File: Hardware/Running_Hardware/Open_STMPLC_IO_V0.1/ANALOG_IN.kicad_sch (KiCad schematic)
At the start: 1 part, among them U39 AD4111

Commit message: Analog input section
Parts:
- added C64, C65, C82: 1uF, symbol Device:C_Small
- added C66, C67, C68, C81: 100nF, symbol Device:C_Small
- added C69, C74, C79, C80: 4.7nF, symbol Device:C_Small
- added C70, C73, C77, C78: 680pF, symbol Device:C_Small
- added C71, C72, C75, C76: 470pF, symbol Device:C_Small
- added C83, C84: 10pF, Capacitor_SMD:C_0603_1608Metric_Pad1.08x0.95mm_HandSolder, symbol Device:C_Small
- added D118, D121, D124, D125: SMAJ33CA, Diode_SMD:D_SMA, symbol Diode:SMAJ33CA
- added D119, D120, D122, D123: SMAJ10CA, Diode_SMD:D_SMA, symbol Diode:SMAJ33CA
- added D126, D127, D128: LED, symbol Device:LED_Small
- added F1, F2, F3, F4: MF-USMF005-2, symbol Device:Fuse_Small
- added J35, J36, J37, J38: Screw_Terminal_01x03, symbol Connector:Screw_Terminal_01x03
- added R190, R191: 0R, symbol Device:R_Small
- added R192, R194, R195, R196, R198, R199, R200, R201: 180R, symbol Device:R_Small
- added R193, R197, R202, R203: 1K, symbol Device:R_Small
- added R204, R205: 100K, symbol Device:R_Small
- added R206: 2.2K, symbol Device:R_Small
- added R207, R208: 4.7K, symbol Device:R_Small
- added TP1, TP2, TP3, TP4, TP5: TestPoint, symbol Connector:TestPoint
- added U40: REF3025, Package_TO_SOT_SMD:SOT-23, symbol Reference_Voltage:REF3025
- added Y2: 16MHz, Crystal:Crystal_SMD_5032-4Pin_5.0x3.2mm, symbol Device:Crystal_GND24
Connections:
- net GND: now reaches U39.1 (VINCOM)
- net GND: now also U39.21 (DGND), U39.30 (IIN3-), U39.31 (IIN2-), U39.32 (IIN1-), U39.33 (IIN0-), U39.41 (EP), U39.8 (AVSS), C64.2, C65.2, C66.2, C67.2, C68.2, C69.2, C71.1, C72.1, C74.2, C75.1, C76.1, C79.2, C80.2, C81.2, C82.2, C83.2, C84.2, D118.2 (A2), D119.1 (A1), D120.1 (A1), D121.2 (A2), D122.1 (A1), D123.1 (A1), D124.2 (A2), D125.2 (A2), J35.1 (Pin_1), J36.1 (Pin_1), J37.1 (Pin_1), J38.1 (Pin_1), R190.2, R191.2, U40.3 (GND), Y2.2, Y2.4
- net at U39.11 (VBIAS-): now also R190.1
- net XTAL1: now reaches U39.12 (XTAL1)
- net XTAL1: now also C83.1, Y2.3
- net XTAL2: now reaches U39.13 (XTAL2/CLKIO)
- net XTAL2: now also C84.1, Y2.1
- net ANALOG_IN_DOUT: now reaches U39.14 (DOUT/~{RDY})
- net ANALOG_IN_DOUT: now also R205.2
- net ANALOG_IN_DIN: now reaches U39.15 (DIN)
- net ANALOG_IN_SCLK: now reaches U39.16 (SCLK)
- net ANALOG_IN_CS: now reaches U39.17 (~{CS})
- net at U39.18 (~{ERROR}): now also D126.1 (K)
- net at U39.19 (~{SYNC}): now also R204.2
- net VIN0: now reaches U39.2 (VIN0)
- net VIN0: now also C69.1, C70.1, R192.1
- net at U39.20 (IOVDD): now also C67.1
- net at U39.22 (REGCAPD): now also C65.1
- net COMPA: now reaches U39.23 (COMPA)
- net COMPA: now also R193.1, R197.1, R202.1, R203.1
- net at U39.24 (COMPB): now also TP1.1
- net at U39.25 (GPO0): now also D127.1 (K)
- net VIN4: now reaches U39.26 (VIN4)
- net VIN4: now also C77.1, C79.1, R200.1
- net at U39.27 (VIN5): now also TP4.1
- net VIN6: now reaches U39.28 (VIN6)
- net VIN6: now also C78.1, C80.1, R201.1
- net at U39.29 (VIN7): now also TP5.1
- net at U39.3 (VIN1): now also TP2.1
- net IIN0+: now reaches U39.34 (IIN0+)
- net IIN0+: now also C71.2, R194.1
- net IIN1+: now reaches U39.35 (IIN1+)
- net IIN1+: now also C72.2, R195.1
- net IIN2+: now reaches U39.36 (IIN2+)
- net IIN2+: now also C75.2, R198.1
- net IIN3+: now reaches U39.37 (IIN3+)
- net IIN3+: now also C76.2, R199.1
- net at U39.38 (GPO1): now also D128.1 (K)
- net at U39.39 (REF-): now also R191.1
- net VIN2: now reaches U39.4 (VIN2)
- net VIN2: now also C73.1, C74.1, R196.1
- net REF+: now reaches U39.40 (REF+)
- net REF+: now also C81.1, C82.1, U40.2 (OUT)
- net at U39.5 (VIN3): now also TP3.1
- net at U39.6 (REFOUT): now also C68.1
- net at U39.7 (REGCAPA): now also C64.1
- net at U39.9 (AVDD): now also C66.1
- new net: C70.2, R193.2
- new net: D122.2 (A2), F3.2, R198.2
- new net: F3.1, J37.3 (Pin_3)
- new net: D125.1 (A1), J38.2 (Pin_2), R201.2
- new net: F4.1, J38.3 (Pin_3)
- new net: F2.1, J36.3 (Pin_3)
- new net: D120.2 (A2), F2.2, R195.2
- new net: C73.2, R197.2
- new net: C77.2, R202.2
- new net: D119.2 (A2), F1.2, R194.2
- new net: C78.2, R203.2
- new net: D127.2 (A), R207.2
- new net: D121.1 (A1), J36.2 (Pin_2), R196.2
- new net: D123.2 (A2), F4.2, R199.2
- new net: D124.1 (A1), J37.2 (Pin_2), R200.2
- new net: D126.2 (A), R206.2
- new net: D128.2 (A), R208.2
- new net: F1.1, J35.3 (Pin_3)
- new net: D118.1 (A1), J35.2 (Pin_2), R192.2
- new net +3V3: R204.1, R205.1, R206.1, R207.1, R208.1, U40.1 (IN)
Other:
- moved on the sheet: U39

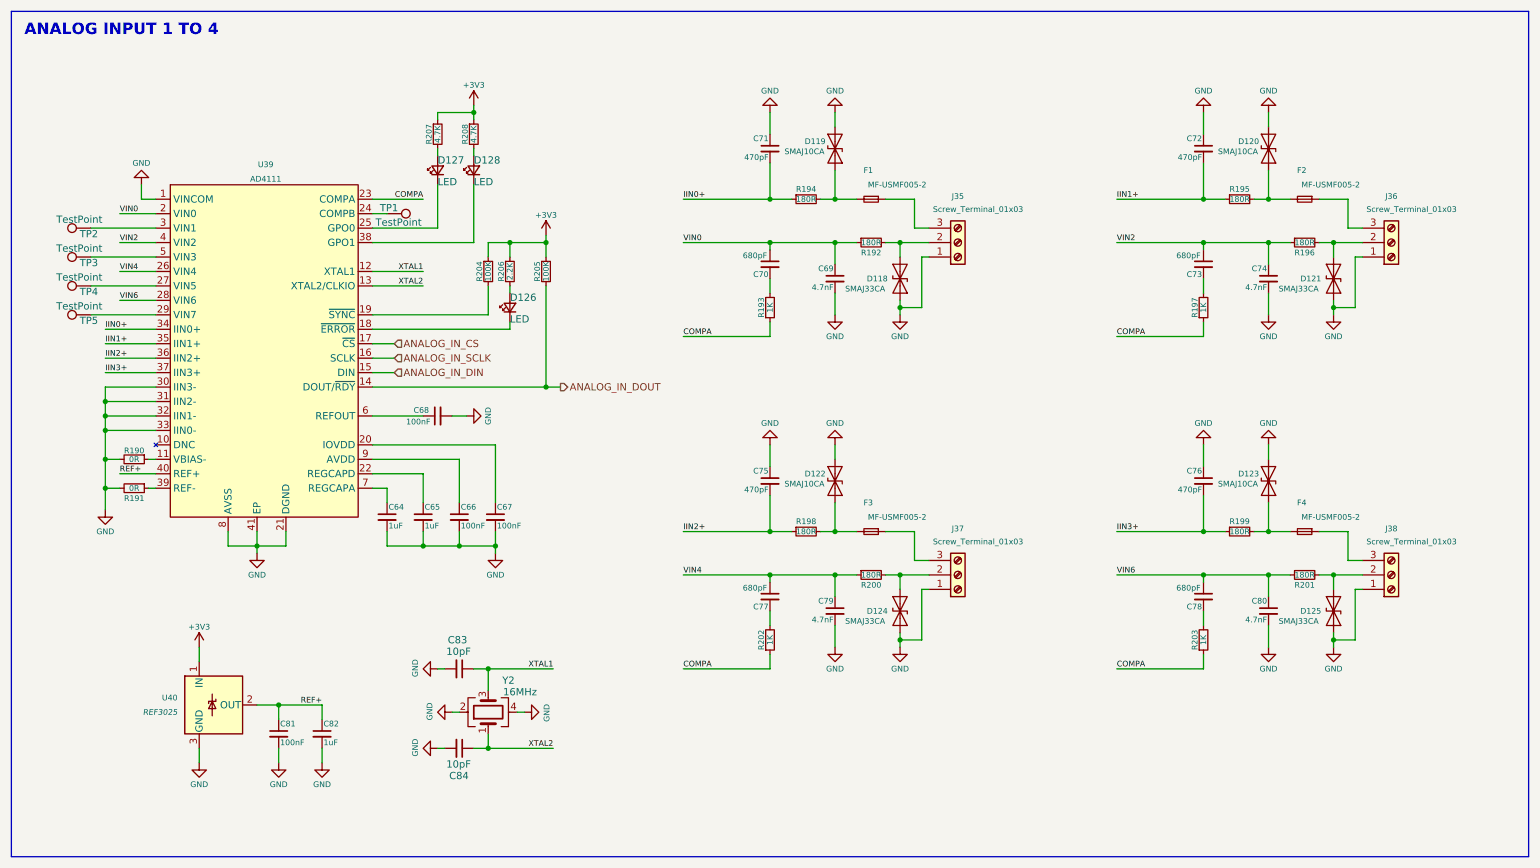
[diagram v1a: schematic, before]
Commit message: GSM Module add
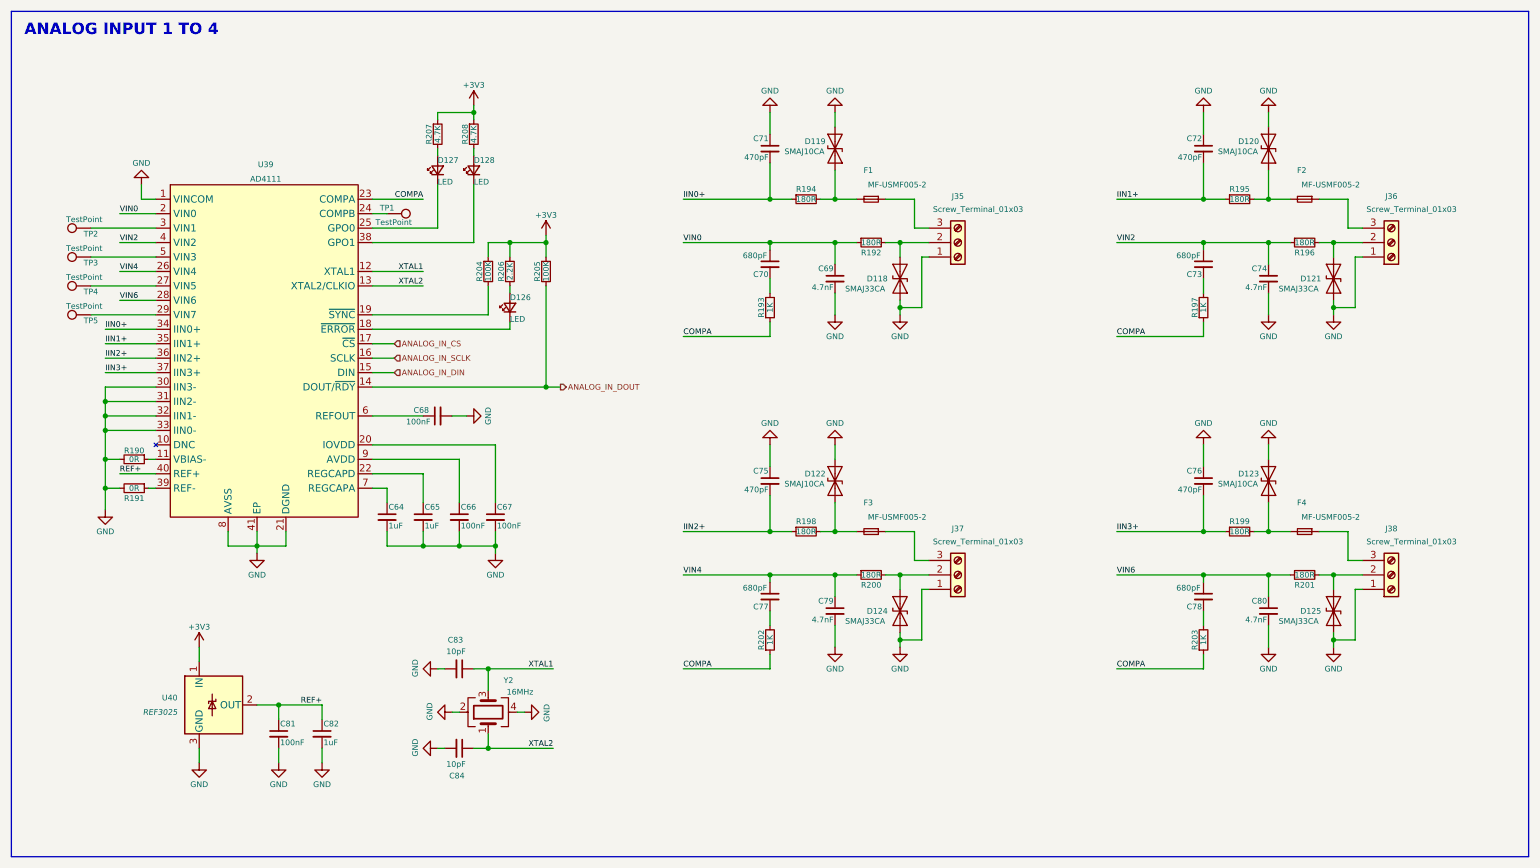
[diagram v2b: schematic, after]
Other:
- title: (none) -> Open_PLC_IO
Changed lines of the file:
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@@
 	(generator_version "9.0")
 	(paper "A4")
+	(title_block
+		(title "Open_PLC_IO")
+		(date "2026-04-01")
+		(rev "0.1")
+	)
 	(rectangle
 		(start 15.24 13.97)
@@
 		(effects
 			(font
-				(size 1.27 1.27)
+				(size 1 1)
 			)
 			(justify left)
@@
 		(effects
 			(font
-				(size 1.27 1.27)
+				(size 1 1)
 			)
 			(justify left)
@@
 		(effects
 			(font
-				(size 1.27 1.27)
+				(size 1 1)
 			)
 			(justify left)
@@
 		(effects
 			(font
-				(size 1.27 1.27)
+				(size 1 1)
 			)
 			(justify left)
@@
 			(effects
 				(font
-					(size 1.27 1.27)
+					(size 1 1)
 				)
 				(justify left)
@@
 			(effects
 				(font
-					(size 1.27 1.27)
+					(size 1 1)
 				)
 				(justify left)
@@
 			(effects
 				(font
-					(size 1.27 1.27)
+					(size 1 1)
 				)
 				(justify left)
@@
 			(effects
 				(font
-					(size 1.27 1.27)
+					(size 1 1)
 				)
 				(justify left)
@@
 			(effects
 				(font
-					(size 1.27 1.27)
+					(size 1 1)
 				)
 				(justify left)
@@
 			(effects
 				(font
-					(size 1.27 1.27)
+					(size 1 1)
 				)
 				(justify left)
@@
 			(effects
 				(font
-					(size 1.27 1.27)
+					(size 1 1)
 				)
 				(justify left)
@@
 			(effects
 				(font
-					(size 1.27 1.27)
+					(size 1 1)
 				)
 				(justify left)
@@
 			(effects
 				(font
-					(size 1.27 1.27)
+					(size 1 1)
 				)
 				(justify right)
@@
 			(effects
 				(font
-					(size 1.27 1.27)
+					(size 1 1)
 				)
 				(justify right)
@@
 			(effects
 				(font
-					(size 1.27 1.27)
+					(size 1 1)
 				)
 				(justify left)
@@
 			(effects
 				(font
-					(size 1.27 1.27)
+					(size 1 1)
 				)
 				(justify left)
@@
 			(effects
 				(font
-					(size 1.27 1.27)
+					(size 1 1)
 				)
 				(justify right)
@@
 			(effects
 				(font
-					(size 1.27 1.27)
+					(size 1 1)
 				)
 				(justify right)
@@
 			(effects
 				(font
-					(size 1.27 1.27)
+					(size 1 1)
 				)
 				(justify left)
@@
 			(effects
 				(font
-					(size 1.27 1.27)
+					(size 1 1)
 				)
 				(justify left)
@@
 			(effects
 				(font
-					(size 1.27 1.27)
+					(size 1 1)
 				)
 				(justify right)
@@
 			(effects
 				(font
-					(size 1.27 1.27)
+					(size 1 1)
 				)
 				(justify right)
@@
 			(effects
 				(font
-					(size 1.27 1.27)
+					(size 1 1)
 				)
 			)
@@
 			(effects
 				(font
-					(size 1.27 1.27)
+					(size 1 1)
 				)
 			)
@@
 			(effects
 				(font
-					(size 1.27 1.27)
+					(size 1 1)
 				)
 				(justify left)
@@
 			(effects
 				(font
-					(size 1.27 1.27)
+					(size 1 1)
 				)
 				(justify left)

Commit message: Main PCB schematic changes V0.1
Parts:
- C64, C65, C66, C67, C68, C69, C70, C71, C72, C73, C74, C75, C76, C77, C78, C79, C80, C81, C82: footprint (none) -> Capacitor_SMD:C_0603_1608Metric_Pad1.08x0.95mm_HandSolder
- D126, D127, D128: footprint (none) -> LED_SMD:LED_0603_1608Metric_Pad1.05x0.95mm_HandSolder
- F1, F2, F3, F4: footprint (none) -> Fuse:Fuse_1210_3225Metric
- J35, J36, J37, J38: footprint (none) -> TerminalBlock_Phoenix:TerminalBlock_Phoenix_MKDS-1,5-3-5.08_1x03_P5.08mm_Horizontal
- R190, R191, R192, R193, R194, R195, R196, R197, R198, R199, R200, R201, R202, R203, R204, R205, R206, R207, R208: footprint (none) -> Resistor_SMD:R_0603_1608Metric_Pad0.98x0.95mm_HandSolder
- TP1, TP2, TP3, TP4, TP5: footprint (none) -> TestPoint:TestPoint_Pad_D1.0mm
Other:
- title: Open_PLC_IO -> Open_STMPLC_IO
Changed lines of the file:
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@@
 	(paper "A4")
 	(title_block
-		(title "Open_PLC_IO")
-		(date "2026-04-01")
+		(title "Open_STMPLC_IO")
+		(date "2026-04-04")
 		(rev "0.1")
 	)
@@
 			)
 		)
-		(property "Footprint" ""
+		(property "Footprint" "Capacitor_SMD:C_0603_1608Metric_Pad1.08x0.95mm_HandSolder"
 			(at 148.59 58.42 0)
 			(effects
@@
 			)
 		)
-		(property "Footprint" ""
+		(property "Footprint" "Capacitor_SMD:C_0603_1608Metric_Pad1.08x0.95mm_HandSolder"
 			(at 81.28 102.87 0)
 			(effects
@@
 			)
 		)
-		(property "Footprint" ""
+		(property "Footprint" "Capacitor_SMD:C_0603_1608Metric_Pad1.08x0.95mm_HandSolder"
 			(at 69.85 140.97 0)
 			(effects
@@
 			)
 		)
-		(property "Footprint" ""
+		(property "Footprint" "Fuse:Fuse_1210_3225Metric"
 			(at 166.37 105.41 0)
 			(effects
@@
 			)
 		)
-		(property "Footprint" ""
+		(property "Footprint" "TestPoint:TestPoint_Pad_D1.0mm"
 			(at 29.21 46.99 0)
 			(effects
@@
 			)
 		)
-		(property "Footprint" ""
+		(property "Footprint" "TerminalBlock_Phoenix:TerminalBlock_Phoenix_MKDS-1,5-3-5.08_1x03_P5.08mm_Horizontal"
 			(at 257.81 113.03 0)
 			(effects
@@
 			)
 		)
-		(property "Footprint" ""
+		(property "Footprint" "Fuse:Fuse_1210_3225Metric"
 			(at 242.57 46.99 0)
 			(effects
@@
 			)
 		)
-		(property "Footprint" ""
+		(property "Footprint" "Capacitor_SMD:C_0603_1608Metric_Pad1.08x0.95mm_HandSolder"
 			(at 224.79 58.42 0)
 			(effects
@@
 			)
 		)
-		(property "Footprint" ""
+		(property "Footprint" "Capacitor_SMD:C_0603_1608Metric_Pad1.08x0.95mm_HandSolder"
 			(at 148.59 116.84 0)
 			(effects
@@
 			)
 		)
-		(property "Footprint" ""
+		(property "Footprint" "Resistor_SMD:R_0603_1608Metric_Pad0.98x0.95mm_HandSolder"
 			(at 154.94 46.99 0)
 			(effects
@@
 			)
 		)
-		(property "Footprint" ""
+		(property "Footprint" "Capacitor_SMD:C_0603_1608Metric_Pad1.08x0.95mm_HandSolder"
 			(at 62.23 140.97 0)
 			(effects
@@
 			)
 		)
-		(property "Footprint" ""
+		(property "Footprint" "Resistor_SMD:R_0603_1608Metric_Pad0.98x0.95mm_HandSolder"
 			(at 224.79 124.46 0)
 			(effects
@@
 			)
 		)
-		(property "Footprint" ""
+		(property "Footprint" "Resistor_SMD:R_0603_1608Metric_Pad0.98x0.95mm_HandSolder"
 			(at 90.17 35.56 0)
 			(effects
@@
 			)
 		)
-		(property "Footprint" ""
+		(property "Footprint" "TerminalBlock_Phoenix:TerminalBlock_Phoenix_MKDS-1,5-3-5.08_1x03_P5.08mm_Horizontal"
 			(at 257.81 54.61 0)
 			(effects
@@
 			)
 		)
-		(property "Footprint" ""
+		(property "Footprint" "Capacitor_SMD:C_0603_1608Metric_Pad1.08x0.95mm_HandSolder"
 			(at 224.79 96.52 0)
 			(effects
@@
 			)
 		)
-		(property "Footprint" ""
+		(property "Footprint" "Resistor_SMD:R_0603_1608Metric_Pad0.98x0.95mm_HandSolder"
 			(at 109.22 59.69 0)
 			(effects
@@
 			)
 		)
-		(property "Footprint" ""
+		(property "Footprint" "Resistor_SMD:R_0603_1608Metric_Pad0.98x0.95mm_HandSolder"
 			(at 242.57 113.03 0)
 			(effects
@@
 			)
 		)
-		(property "Footprint" ""
+		(property "Footprint" "TestPoint:TestPoint_Pad_D1.0mm"
 			(at 29.21 52.07 0)
 			(effects
@@
 			)
 		)
-		(property "Footprint" ""
+		(property "Footprint" "Resistor_SMD:R_0603_1608Metric_Pad0.98x0.95mm_HandSolder"
 			(at 242.57 54.61 0)
 			(effects
@@
 			)
 		)
-		(property "Footprint" ""
+		(property "Footprint" "TestPoint:TestPoint_Pad_D1.0mm"
 			(at 29.21 62.23 0)
 			(effects
@@
 			)
 		)
-		(property "Footprint" ""
+		(property "Footprint" "Capacitor_SMD:C_0603_1608Metric_Pad1.08x0.95mm_HandSolder"
 			(at 90.17 85.09 0)
 			(effects
@@
 			)
 		)
-		(property "Footprint" ""
+		(property "Footprint" "Capacitor_SMD:C_0603_1608Metric_Pad1.08x0.95mm_HandSolder"
 			(at 87.63 102.87 0)
 			(effects
@@
 			)
 		)
-		(property "Footprint" ""
+		(property "Footprint" "Resistor_SMD:R_0603_1608Metric_Pad0.98x0.95mm_HandSolder"
 			(at 102.87 59.69 0)
 			(effects
@@
 			)
 		)
-		(property "Footprint" ""
+		(property "Footprint" "Resistor_SMD:R_0603_1608Metric_Pad0.98x0.95mm_HandSolder"
 			(at 148.59 66.04 0)
 			(effects
@@
 			)
 		)
-		(property "Footprint" ""
+		(property "Footprint" "Resistor_SMD:R_0603_1608Metric_Pad0.98x0.95mm_HandSolder"
 			(at 154.94 105.41 0)
 			(effects
@@
 			)
 		)
-		(property "Footprint" ""
+		(property "Footprint" "Capacitor_SMD:C_0603_1608Metric_Pad1.08x0.95mm_HandSolder"
 			(at 93.98 102.87 0)
 			(effects
@@
 			)
 		)
-		(property "Footprint" ""
+		(property "Footprint" "LED_SMD:LED_0603_1608Metric_Pad1.05x0.95mm_HandSolder"
 			(at 96.52 41.91 90)
 			(effects
@@
 			)
 		)
-		(property "Footprint" ""
+		(property "Footprint" "Capacitor_SMD:C_0603_1608Metric_Pad1.08x0.95mm_HandSolder"
 			(at 160.02 119.38 0)
 			(effects
@@
 			)
 		)
-		(property "Footprint" ""
+		(property "Footprint" "Resistor_SMD:R_0603_1608Metric_Pad0.98x0.95mm_HandSolder"
 			(at 231.14 105.41 0)
 			(effects
@@
 			)
 		)
-		(property "Footprint" ""
+		(property "Footprint" "LED_SMD:LED_0603_1608Metric_Pad1.05x0.95mm_HandSolder"
 			(at 102.87 66.04 90)
 			(effects
@@
 			)
 		)
-		(property "Footprint" ""
+		(property "Footprint" "Resistor_SMD:R_0603_1608Metric_Pad0.98x0.95mm_HandSolder"
 			(at 148.59 124.46 0)
 			(effects
@@
 			)
 		)
-		(property "Footprint" ""
+		(property "Footprint" "Capacitor_SMD:C_0603_1608Metric_Pad1.08x0.95mm_HandSolder"
 			(at 160.02 60.96 0)
 			(effects
@@
 			)
 		)
-		(property "Footprint" ""
+		(property "Footprint" "Capacitor_SMD:C_0603_1608Metric_Pad1.08x0.95mm_HandSolder"
 			(at 224.79 116.84 0)
 			(effects
@@
 			)
 		)
-		(property "Footprint" ""
+		(property "Footprint" "Resistor_SMD:R_0603_1608Metric_Pad0.98x0.95mm_HandSolder"
 			(at 96.52 35.56 0)
 			(effects
@@
 			)
 		)
-		(property "Footprint" ""
+		(property "Footprint" "Fuse:Fuse_1210_3225Metric"
 			(at 166.37 46.99 0)
 			(effects
@@
 			)
 		)
-		(property "Footprint" ""
+		(property "Footprint" "Resistor_SMD:R_0603_1608Metric_Pad0.98x0.95mm_HandSolder"
 			(at 36.83 92.71 0)
 			(effects
@@
 			)
 		)
-		(property "Footprint" ""
+		(property "Footprint" "TerminalBlock_Phoenix:TerminalBlock_Phoenix_MKDS-1,5-3-5.08_1x03_P5.08mm_Horizontal"
 			(at 181.61 113.03 0)
 			(effects
@@
 			)
 		)
-		(property "Footprint" ""
+		(property "Footprint" "Capacitor_SMD:C_0603_1608Metric_Pad1.08x0.95mm_HandSolder"
 			(at 236.22 60.96 0)
 			(effects
@@
 			)
 		)
-		(property "Footprint" ""
+		(property "Footprint" "Resistor_SMD:R_0603_1608Metric_Pad0.98x0.95mm_HandSolder"
 			(at 231.14 46.99 0)
 			(effects
@@
 			)
 		)
-		(property "Footprint" ""
+		(property "Footprint" "Resistor_SMD:R_0603_1608Metric_Pad0.98x0.95mm_HandSolder"
 			(at 224.79 66.04 0)
 			(effects
@@
 			)
 		)
-		(property "Footprint" ""
+		(property "Footprint" "TestPoint:TestPoint_Pad_D1.0mm"
 			(at 81.28 54.61 0)
 			(effects
@@
 			)
 		)
-		(property "Footprint" ""
+		(property "Footprint" "Capacitor_SMD:C_0603_1608Metric_Pad1.08x0.95mm_HandSolder"
 			(at 224.79 38.1 0)
 			(effects
@@
 			)
 		)
-		(property "Footprint" ""
+		(property "Footprint" "Resistor_SMD:R_0603_1608Metric_Pad0.98x0.95mm_HandSolder"
 			(at 166.37 54.61 0)
 			(effects
@@
 			)
 		)
-		(property "Footprint" ""
+		(property "Footprint" "LED_SMD:LED_0603_1608Metric_Pad1.05x0.95mm_HandSolder"
 			(at 90.17 41.91 90)
 			(effects
@@
 			)
 		)
-		(property "Footprint" ""
+		(property "Footprint" "Resistor_SMD:R_0603_1608Metric_Pad0.98x0.95mm_HandSolder"
 			(at 36.83 97.79 0)
 			(effects
@@
 			)
 		)
-		(property "Footprint" ""
+		(property "Footprint" "Capacitor_SMD:C_0603_1608Metric_Pad1.08x0.95mm_HandSolder"
 			(at 148.59 96.52 0)
 			(effects
@@
 			)
 		)
-		(property "Footprint" ""
+		(property "Footprint" "TerminalBlock_Phoenix:TerminalBlock_Phoenix_MKDS-1,5-3-5.08_1x03_P5.08mm_Horizontal"
 			(at 181.61 54.61 0)
 			(effects
@@
 			)
 		)
-		(property "Footprint" ""
+		(property "Footprint" "Fuse:Fuse_1210_3225Metric"
 			(at 242.57 105.41 0)
 			(effects
@@
 			)
 		)
-		(property "Footprint" ""
+		(property "Footprint" "Capacitor_SMD:C_0603_1608Metric_Pad1.08x0.95mm_HandSolder"
 			(at 100.33 102.87 0)
 			(effects
@@
 			)
 		)
-		(property "Footprint" ""
+		(property "Footprint" "Capacitor_SMD:C_0603_1608Metric_Pad1.08x0.95mm_HandSolder"
 			(at 148.59 38.1 0)
 			(effects
@@
 			)
 		)
-		(property "Footprint" ""
+		(property "Footprint" "Resistor_SMD:R_0603_1608Metric_Pad0.98x0.95mm_HandSolder"
 			(at 99.06 59.69 0)
 			(effects
@@
 			)
 		)
-		(property "Footprint" ""
+		(property "Footprint" "Resistor_SMD:R_0603_1608Metric_Pad0.98x0.95mm_HandSolder"
 			(at 166.37 113.03 0)
 			(effects
@@
 			)
 		)
-		(property "Footprint" ""
+		(property "Footprint" "Capacitor_SMD:C_0603_1608Metric_Pad1.08x0.95mm_HandSolder"
 			(at 236.22 119.38 0)
 			(effects
@@
 			)
 		)
-		(property "Footprint" ""
+		(property "Footprint" "TestPoint:TestPoint_Pad_D1.0mm"
 			(at 29.21 57.15 0)
 			(effects
